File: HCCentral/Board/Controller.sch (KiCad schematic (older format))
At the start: 29 parts, among them CON2 SD_Card, IC2 ATMEGA1284P-A, P4 ISP, P6 SPI, P7 UART, SW1 Reset, SW2 SW_PUSH, Y2 16MHz

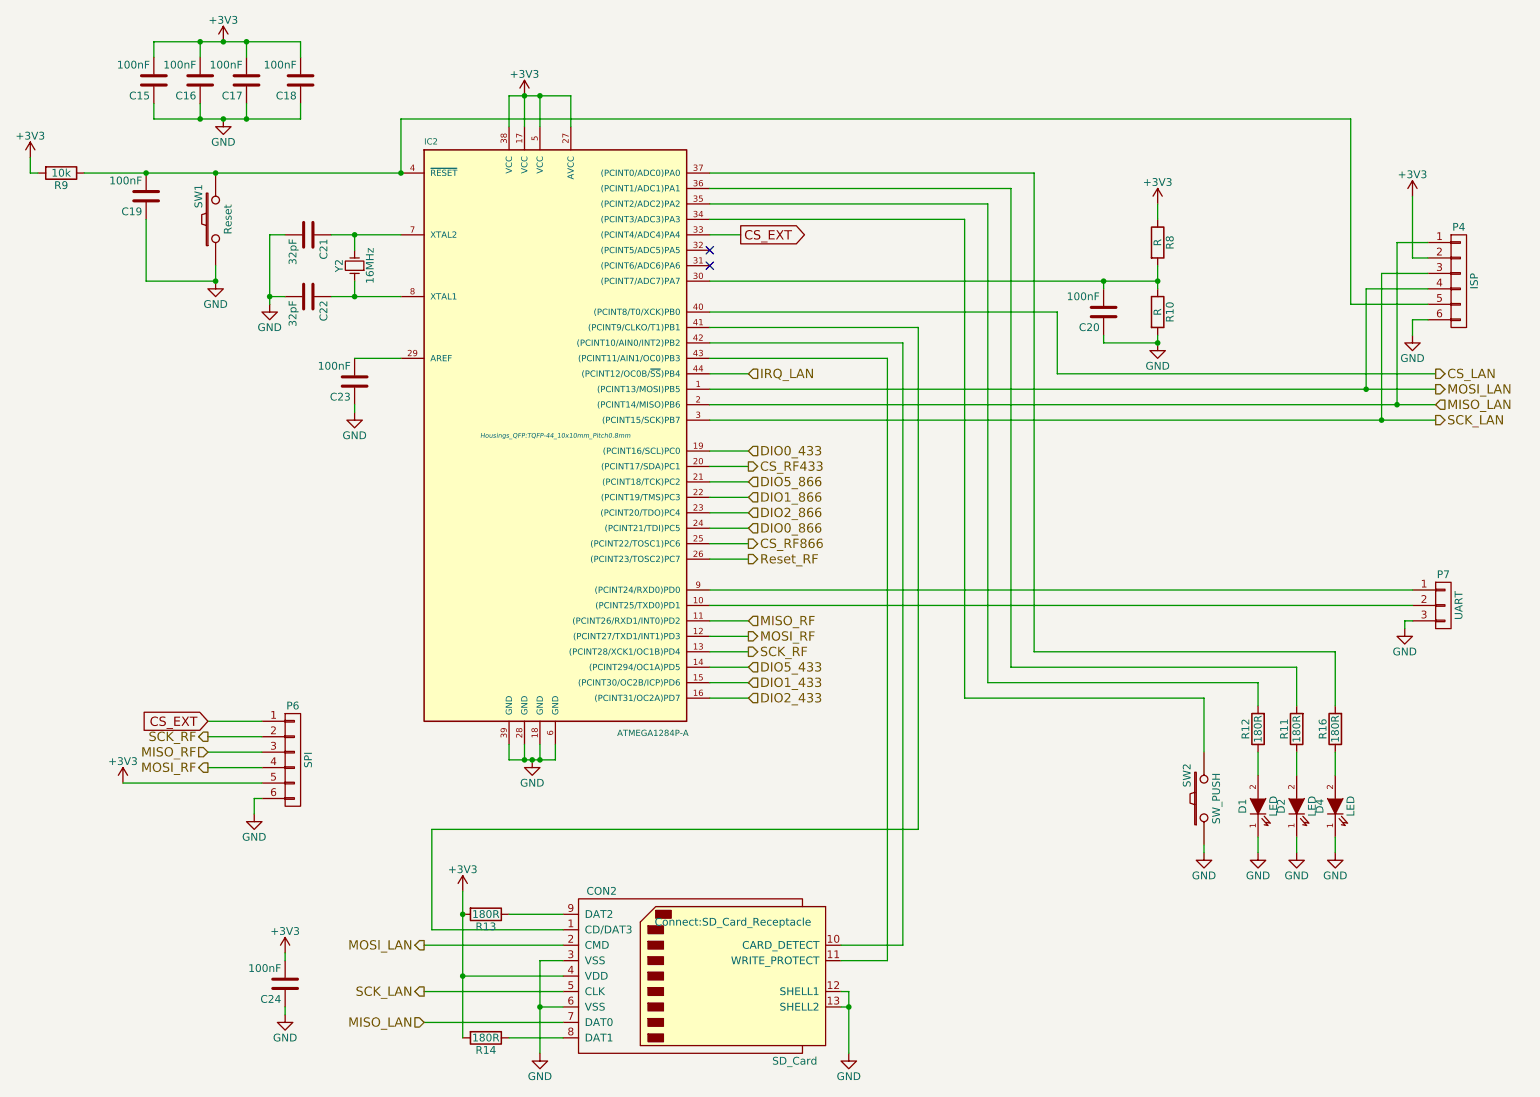
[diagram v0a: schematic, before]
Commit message: Deleted Gerbers, Updated V1.5
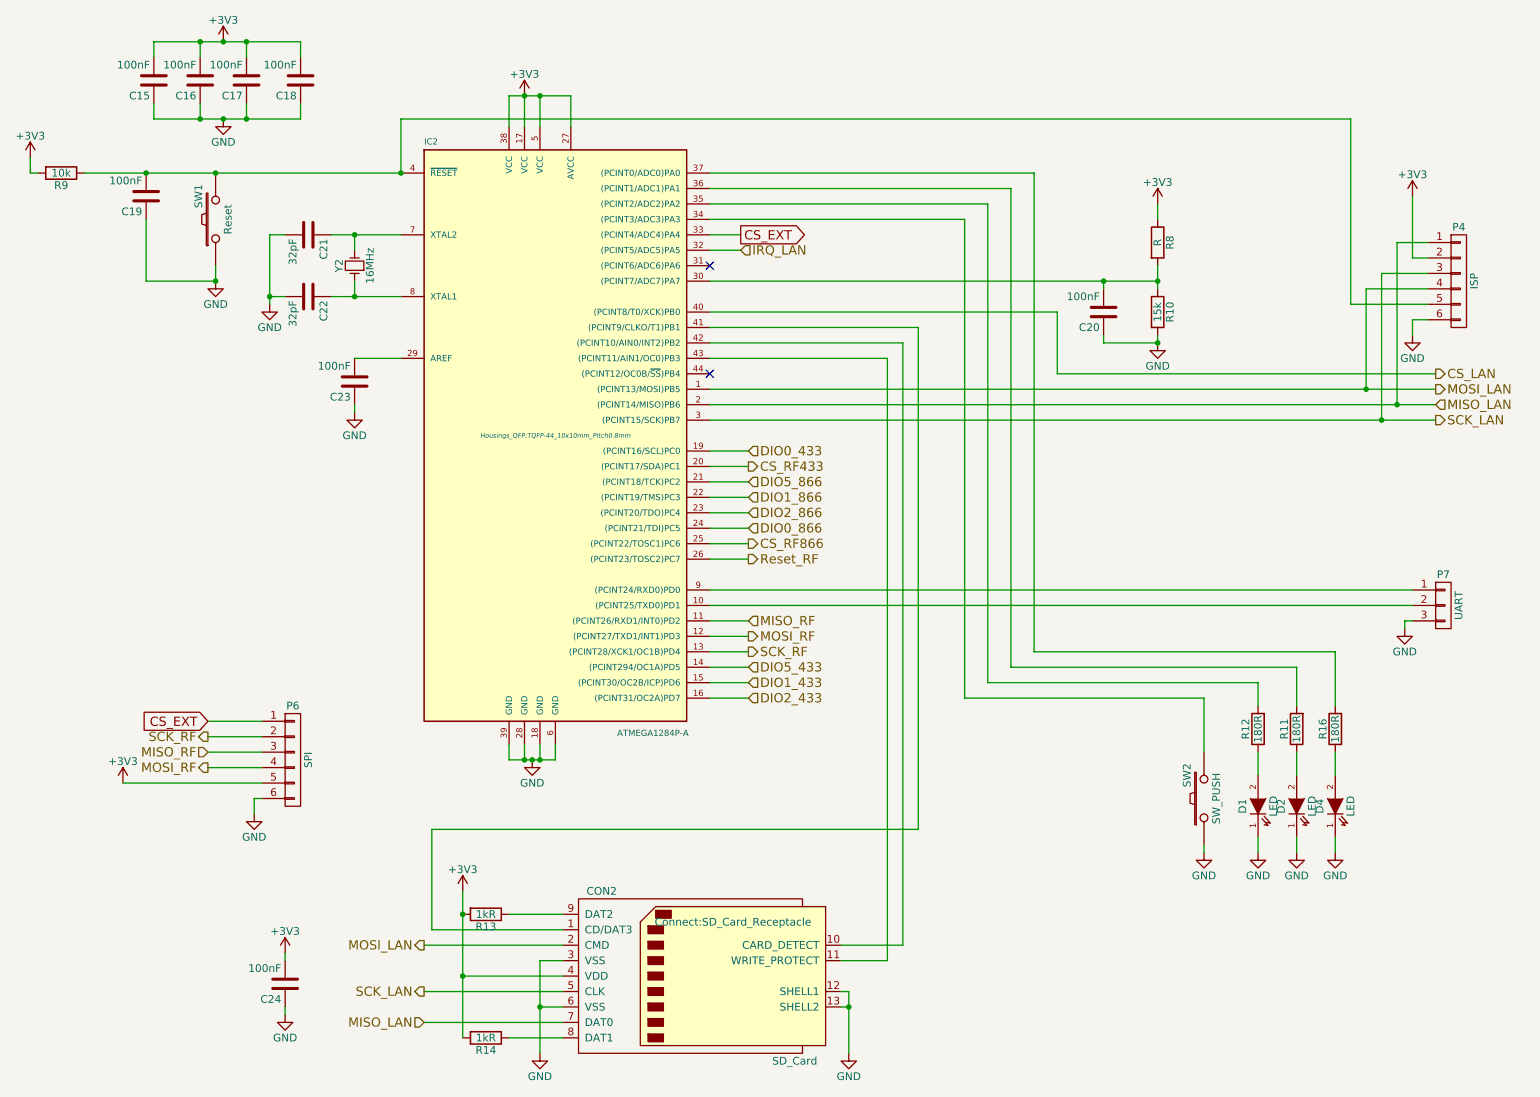
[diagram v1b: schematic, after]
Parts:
- R10: value R -> 15k
- R13, R14: value 180R -> 1kR
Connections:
- net IRQ_LAN: now also IC2.32 ((PCINT5/ADC5)PA5); no longer IC2.44 ((PCINT12/OC0B/~SS~)PB4)
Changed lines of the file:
@@
 	1    0    0    -1
 $EndComp
-Text HLabel 5650 2950 2    60   Input ~ 0
+Text HLabel 5600 2150 2    60   Input ~ 0
 IRQ_LAN
 $Comp
@@
 P 8300 2550
 F 0 "R10" V 8380 2550 50  0000 C CNN
-F 1 "R" V 8300 2550 50  0000 C CNN
+F 1 "15k" V 8300 2550 50  0000 C CNN
 F 2 "Resistors_SMD:R_0805" V 8230 2550 30  0001 C CNN
 F 3 "" H 8300 2550 30  0000 C CNN
@@
 P 3950 6450
 F 0 "R13" V 4030 6450 50  0000 C CNN
-F 1 "180R" V 3950 6450 50  0000 C CNN
+F 1 "1kR" V 3950 6450 50  0000 C CNN
 F 2 "Resistors_SMD:R_0805" V 3880 6450 30  0001 C CNN
 F 3 "" H 3950 6450 30  0000 C CNN
@@
 P 3950 7250
 F 0 "R14" V 4030 7250 50  0000 C CNN
-F 1 "180R" V 3950 7250 50  0000 C CNN
+F 1 "1kR" V 3950 7250 50  0000 C CNN
 F 2 "Resistors_SMD:R_0805" V 3880 7250 30  0001 C CNN
 F 3 "" H 3950 7250 30  0000 C CNN
@@
 	5400 2350 8300 2350
 Wire Wire Line
-	5400 2950 5650 2950
-Wire Wire Line
 	6550 2850 5400 2850
 Wire Wire Line
@@
 	8600 5050 8600 5400
 NoConn ~ 5400 2250
-NoConn ~ 5400 2150
 Wire Wire Line
 	9550 2500 10050 2500
@@
 Wire Wire Line
 	5400 2050 5600 2050
+Wire Wire Line
+	5400 2150 5600 2150
+NoConn ~ 5400 2950
 $EndSCHEMATC
